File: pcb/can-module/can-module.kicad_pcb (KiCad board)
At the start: 2 copper layers, 55.8 x 91.5 mm, 103 parts, among them J10 MKDS-1,5-2-5.08, J11 MKDS-1,5-2-5.08, J12 MKDS-1,5-2-5.08, J13 MKDS-1,5-2-5.08, J14 MKDS-1,5-2-5.08, J16 USB4105, J17 Conn_01x18, J18 Conn_01x18, J3 TC2050, J4 MKDS-1,5-2-5.08, J6 MKDS-1,5-2-5.08, J7 MKDS-1,5-2-5.08, J8 MKDS-1,5-2-5.08, J9 MKDS-1,5-2-5.08, Q10 2N7002, Q11 AO3401A, Q12 2N7002, Q13 2N7002, Q14 AO3401A, Q15 2N7002, Q4 2N7002, Q5 AO3401A, Q6 2N7002, Q7 2N7002, Q8 AO3401A, Q9 2N7002, U1 AP2112K-3.3, U2 MCP25625x-x-ML, U3 TPS2116DRL, U4 MCP25625x-x-ML, U6 ADS1115IDGS, U7 L78M05ABDT-TR, U8 W25Q32JVSSIQ TR, U9 RP2040, X2 X322516MOB4SI, Y2 ABM8-272-T3

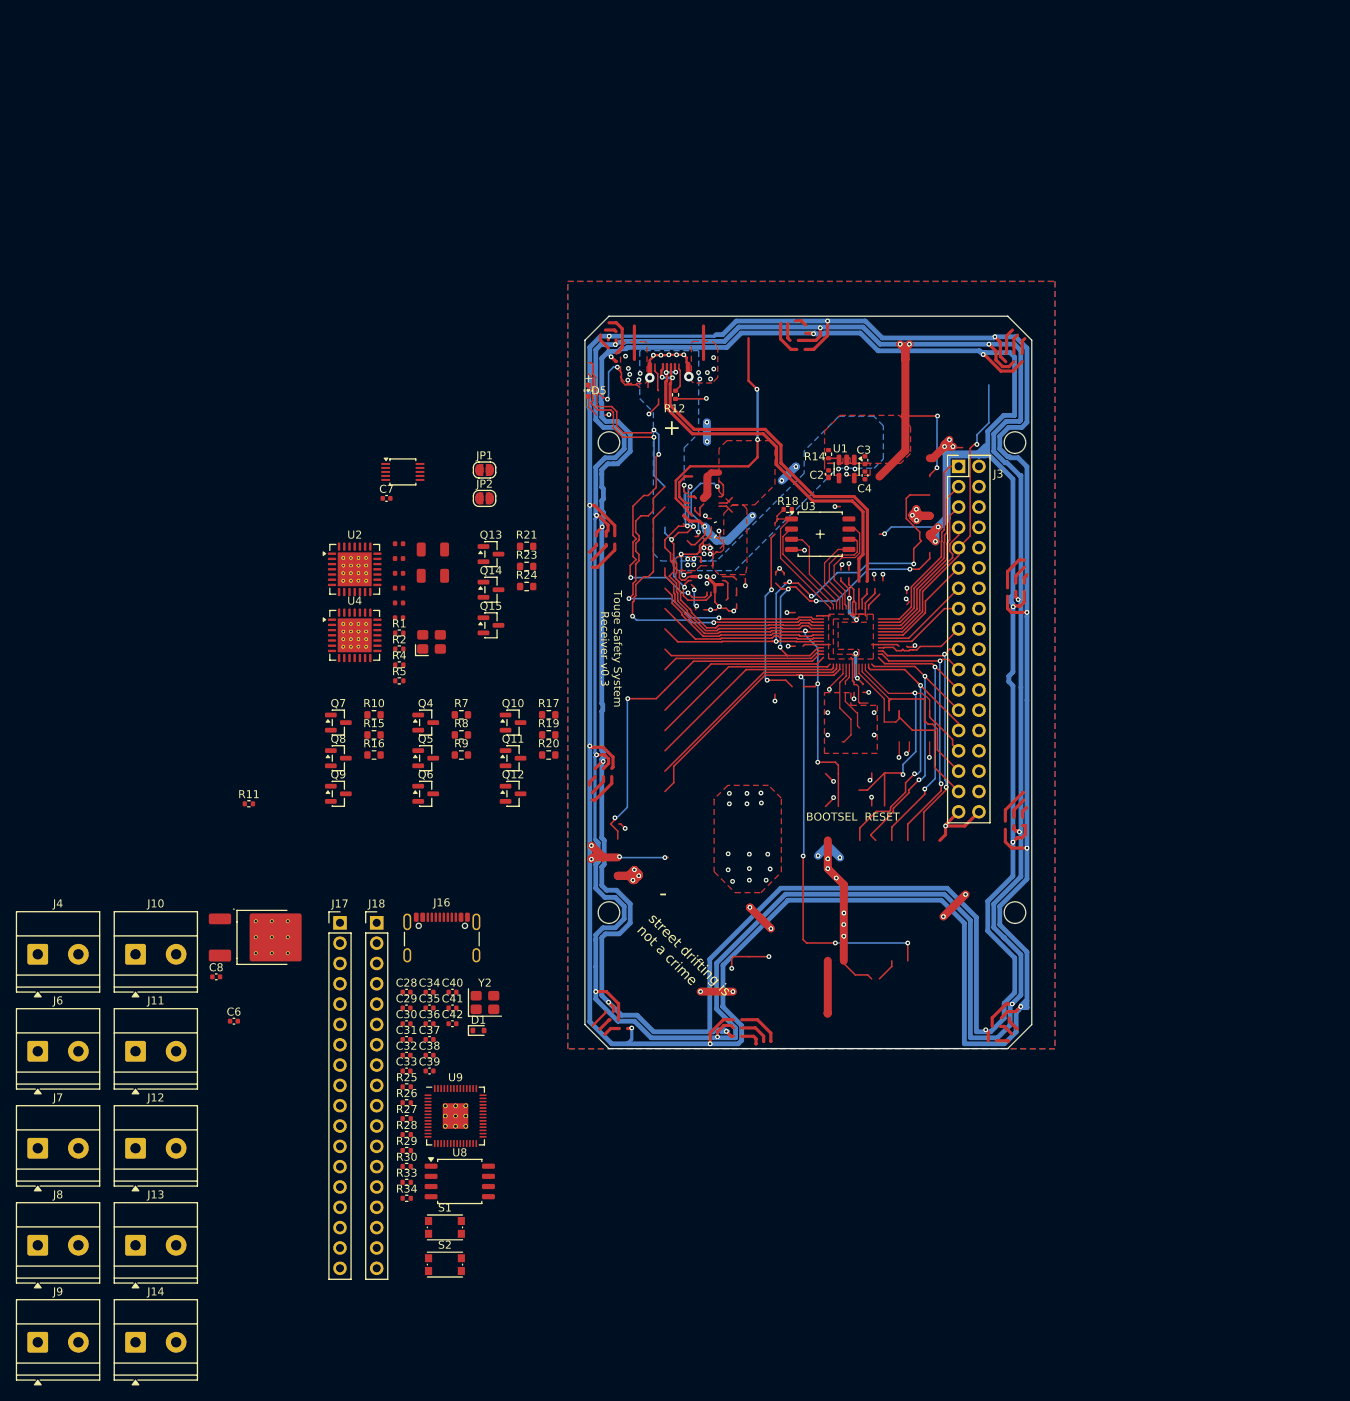
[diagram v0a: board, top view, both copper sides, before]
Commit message: Fix ERC errors
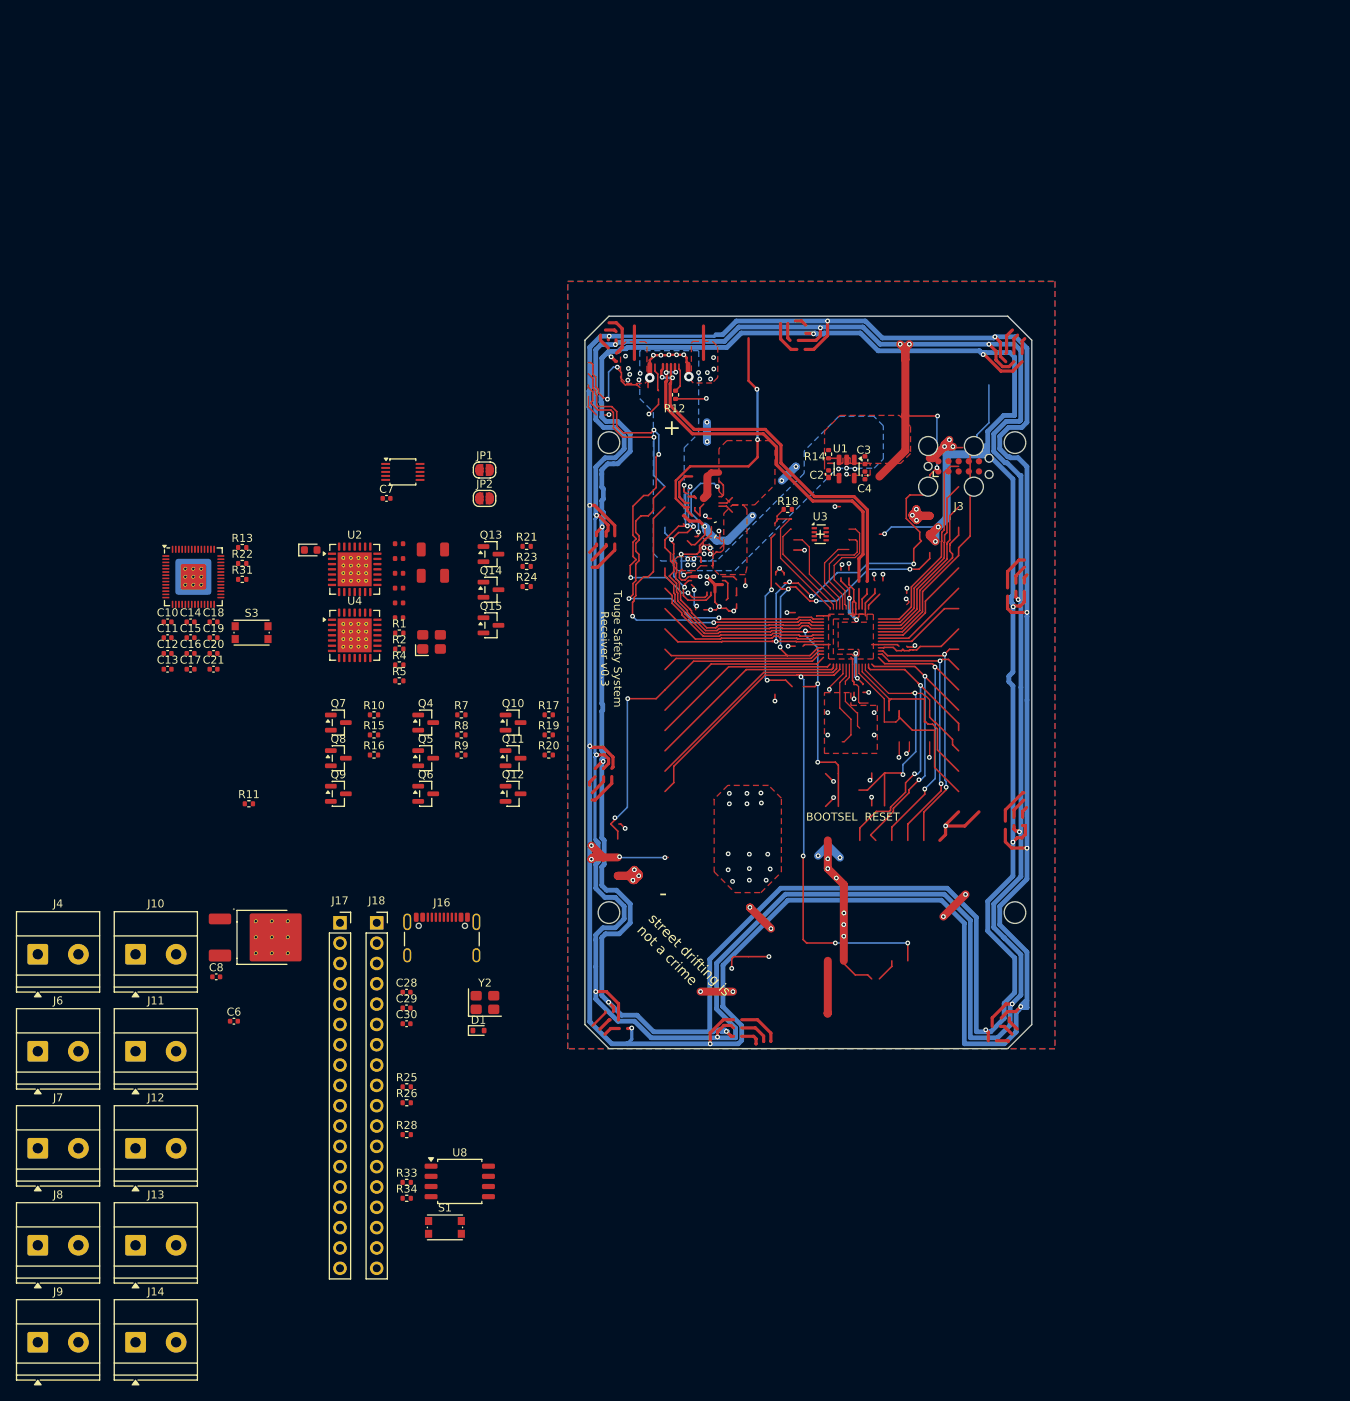
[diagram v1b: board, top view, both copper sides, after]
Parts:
- removed C31, C32, C34, C36, C37, C38, C39, C40, C42: 0.1uF, Capacitor_SMD:C_0402_1005Metric
- removed C33, C35: 1uF, Capacitor_SMD:C_0402_1005Metric
- removed C41: 10uF, Capacitor_SMD:C_0402_1005Metric
- removed D5: Blue LED, Snapeda:WL-SMSW_0603_REC
- removed R27: 10k, Resistor_SMD:R_0402_1005Metric
- removed R29, R30: 27, Resistor_SMD:R_0402_1005Metric
- removed S2: KMR221NG, Button_Switch_SMD:SW_Push_1P1T_NO_CK_KMR2
- removed U9: RP2040, RP2040_minimal:RP2040-QFN-56
- added C10: 0.1uF, Capacitor_SMD:C_0402_1005Metric, F.Cu at (14.6, 98.2)
- added C11: 1uF, Capacitor_SMD:C_0402_1005Metric, F.Cu at (14.6, 100.1)
- added C12: 0.1uF, Capacitor_SMD:C_0402_1005Metric, F.Cu at (14.6, 102.1)
- added C13: 0.1uF, Capacitor_SMD:C_0402_1005Metric, F.Cu at (14.6, 104.1)
- added C14: 0.1uF, Capacitor_SMD:C_0402_1005Metric, F.Cu at (17.4, 98.2)
- added C15: 0.1uF, Capacitor_SMD:C_0402_1005Metric, F.Cu at (17.4, 100.1)
- added C16: 0.1uF, Capacitor_SMD:C_0402_1005Metric, F.Cu at (17.4, 102.1)
- added C17: 0.1uF, Capacitor_SMD:C_0402_1005Metric, F.Cu at (17.4, 104.1)
- added C18: 10uF, Capacitor_SMD:C_0402_1005Metric, F.Cu at (20.3, 98.2)
- added C19: 0.1uF, Capacitor_SMD:C_0402_1005Metric, F.Cu at (20.3, 100.1)
- added C20: 0.1uF, Capacitor_SMD:C_0402_1005Metric, F.Cu at (20.3, 102.1)
- added C21: 1uF, Capacitor_SMD:C_0402_1005Metric, F.Cu at (20.3, 104.1)
- added D2: Blue LED, PCM_JLCPCB:D_0603, F.Cu at (32.5, 89.2)
- added R13: 27, Resistor_SMD:R_0402_1005Metric, F.Cu at (23.9, 88.9)
- added R22: 27, Resistor_SMD:R_0402_1005Metric, F.Cu at (23.9, 90.9)
- added R31: 10k, Resistor_SMD:R_0402_1005Metric, F.Cu at (23.9, 92.8)
- added S3: KMR221NG, Button_Switch_SMD:SW_Push_1P1T_NO_CK_KMR2, F.Cu at (25.1, 99.5)
- added U5: RP2040, PCM_JLCPCB:QFN-56-1EP_7x7mm_P0.4mm_EP3.2x3.2mm_ThermalVias, F.Cu at (17.8, 92.5)
- J17, J18: footprint Connector_PinHeader_2.54mm:PinHeader_1x18_P2.54mm_Vertical -> Connector_PinSocket_2.54mm:PinSocket_1x18_P2.54mm_Vertical
- J3: footprint Connector_PinHeader_2.54mm:PinHeader_2x18_P2.54mm_Vertical -> Connector:Tag-Connect_TC2050-IDC-FP_2x05_P1.27mm_Vertical
- R10, R15, R16, R17, R19, R20, R21, R23, R24, R7, R8, R9: footprint Resistor_SMD:R_0603_1608Metric -> Resistor_SMD:R_0402_1005Metric
- U3: footprint Package_SO:SOIC-8_5.3x5.3mm_P1.27mm -> Package_TO_SOT_SMD:SOT-583-8
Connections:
- net ~{RESET} renamed /PI/~{RESET}
- J17 pad 4: SCL -> SDA
- J17 pad 5: SDA -> SCL
- J3 pad 2: SWD -> /PI/SWD
- J3 pad 4: SWCLK -> /PI/SWCLK
- U2 pad 29: unconnected-(U2-EP-Pad29) -> GND
- U4 pad 29: unconnected-(U4-EP-Pad29) -> GND
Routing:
- net +3V3: track 78.4 -> 443.1 mm, vias 8 -> 22
- net (no net): track 2154.7 -> 1858.2 mm, vias 103 -> 91
- net /PI/~{RESET}: track 40.2 -> 5.87 mm, vias 2 -> 3
- net SWCLK: track 26.4 -> 0.00 mm
- net /PI/SWD: track 0.00 -> 25.4 mm
- net SWD: track 24.2 -> 0.00 mm
- net GND: track 232.3 -> 227.8 mm, vias 96 -> 93
- net Net-(D2-K): track 2.77 -> 0.00 mm
- net Net-(U3-PR1): track 4.97 -> 3.64 mm

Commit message: Board layout
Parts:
- U5: footprint PCM_JLCPCB:QFN-56-1EP_7x7mm_P0.4mm_EP3.2x3.2mm_ThermalVias -> Package_DFN_QFN:QFN-56-1EP_7x7mm_P0.4mm_EP3.2x3.2mm
- moved J4 155.9 mm to (127.8, 85.5), turned to 90 degrees
- moved J3 155.3 mm to (127.8, 74.2), turned to 90 degrees
- moved J7 152.4 mm to (127.8, 107.9), turned to 90 degrees
- moved J8 141.4 mm to (127.8, 119.1), turned to 90 degrees
- moved J9 133.8 mm to (127.8, 130.4), turned to 90 degrees
- moved J11 130.1 mm to (127.8, 152.8), turned to 90 degrees
- moved J10 129.9 mm to (127.8, 141.6), turned to 90 degrees
- moved J1 127.5 mm to (93.4, 67.0), turned to 180 degrees
- moved J2 126.6 mm to (104.6, 67.0), turned to 180 degrees
- moved J5 124.9 mm to (127.8, 96.7), turned to 90 degrees
- moved C2 122.0 mm to (114.4, 67.5), turned to -90 degrees
- moved C1 119.1 mm to (113.2, 67.5), turned to -90 degrees
- moved U1 110.9 mm to (113.8, 71.6), turned to -90 degrees
- moved D2 100.2 mm to (111.4, 150.9), turned to 90 degrees
- moved U8 98.4 mm to (117.3, 145.0), turned to 90 degrees
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- renumbered C8 to C1, C28 to C10, C19 to C11, C14 to C12, C18 to C13, C15 to C14, C13 to C15, C12 to C17, C17 to C18, C11 to C19, C6 to C2, C21 to C20, C20 to C21, C10 to C22, C30 to C23, C7 to C24, C3 to C25, C4 to C26, C2 to C27, C5 to C3, C1 to C4, C24 to C5, C9 to C6, C26 to C7, C25 to C8, C29 to C9, H4 to H1, H1 to H3, H3 to H4, J12 to J1, J6 to J10, J4 to J11, J18 to J12, J17 to J13, J16 to J14, J11 to J2, J13 to J3, J14 to J4, J10 to J5, J3 to J6, J9 to J7, J7 to J9, Q15 to Q1, Q6 to Q10, Q5 to Q11, Q4 to Q12, Q14 to Q2, Q13 to Q3, Q12 to Q4, Q10 to Q5, Q11 to Q6, Q9 to Q7, Q7 to Q9, R3 to R1, R23 to R10, R21 to R11, R20 to R12, R19 to R13, R31 to R14, R17 to R15, R28 to R17, R15 to R18, R10 to R19, R6 to R2, R9 to R20, R8 to R21, R13 to R22, R22 to R23, R7 to R24, R14 to R27, R33 to R28, R34 to R29, R4 to R3, R11 to R30, R12 to R4, R18 to R5, R1 to R6, R2 to R7, R24 to R8, R5 to R9, S3 to S1, S1 to S2, JP1 to TERM_RES_1, JP2 to TERM_RES_2, U7 to U1, U4 to U3, U3 to U4, U8 to U6, U1 to U7, U6 to U8, X2 to X1, Y2 to Y1
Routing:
- net (no net): track 1858.2 -> 0.00 mm, vias 91 -> 0
- net +3V3: track 443.1 -> 50.8 mm, vias 22 -> 8
- net GND: track 227.8 -> 88.5 mm, vias 93 -> 79
- net /USB_VBUS: track 13.0 -> 105.5 mm, vias 0 -> 11
- net +12V: track 0.00 -> 85.2 mm, vias 0 -> 1
- net /Can/CAN_0_RESET: track 37.0 -> 108.4 mm, vias 2 -> 4
- net SCK: track 35.6 -> 105.5 mm, vias 2 -> 5
- net MOSI: track 35.2 -> 104.2 mm, vias 2 -> 4
- net /Can/CAN_1_CS: track 11.5 -> 75.4 mm, vias 0 -> 2
- net MISO: track 35.1 -> 94.4 mm, vias 2 -> 4
- net /Can/CAN_1_INT: track 11.7 -> 69.5 mm, vias 0 -> 2
- net /Can/CAN_1_STBY: track 12.6 -> 69.8 mm, vias 0 -> 2
- net /Can/CAN_1_RESET: track 14.3 -> 70.3 mm, vias 0 -> 3
- net /Can/CAN_0_INT: track 0.00 -> 47.2 mm, vias 0 -> 1
- net /Can/CAN_0_CS: track 0.00 -> 45.8 mm, vias 0 -> 1
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- added copper zone on F.Cu, net +12V
- added copper zone on B.Cu, net /USB_VBUS
- added copper zone on F.Cu, net Net-(U1-VOUT)
- removed copper zone on B.Cu, net (none)
- removed copper zone on F.Cu, net (none)
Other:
- board size 55.8 x 91.5 mm -> 51.6 x 98 mm
- board text added: "+12V IN"
- board text added: "+5V OUT"
- board text added: "AIN0"
- board text added: "AIN1"
- board text added: "AIN2"
- board text added: "AIN3"
- board text added: "CAN_0_H"
- board text added: "CAN_0_L"
- board text added: "CAN_1_H"
- board text added: "CAN_1_L"
- board text added: "GND"
- board text added: "TOTEM_0"
- board text added: "TOTEM_1"
- board text added: "TOTEM_2"
- board text added: "TOTEM_3"
- board text added: "Universal CAN Module v0.1 BD Engineering LLC"
- board text added: "VREF_0"
- board text added: "VREF_1"
- board text added: "VREF_2"
- board text added: "VREF_3"
- board text removed: "Touge Safety System Receiver v0.3"
